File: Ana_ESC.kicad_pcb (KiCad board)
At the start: 4 copper layers, 90 x 90 mm, 105 parts, among them IC3 TCAN330DCNT, J1 BM04B-GHS-TBT_LF__SN__N_, J2 Conn_01x04_Pin, J3 USB_C_Receptacle_USB2.0_16P, J4 BM04B-GHS-TBT_LF__SN__N_, J5 Conn_01x02_Socket, Q10 STL90N6F7, Q11 STL90N6F7, Q12 STL90N6F7, Q7 STL90N6F7, Q8 STL90N6F7, Q9 STL90N6F7, SW1 SW_SPDT, SW2 SW_SPDT, U1 DRV8323RSRGZR, U2 STM32G431CBU6, U3 ME6211C33M5, Y1 ECS-80-20-5PX-TR

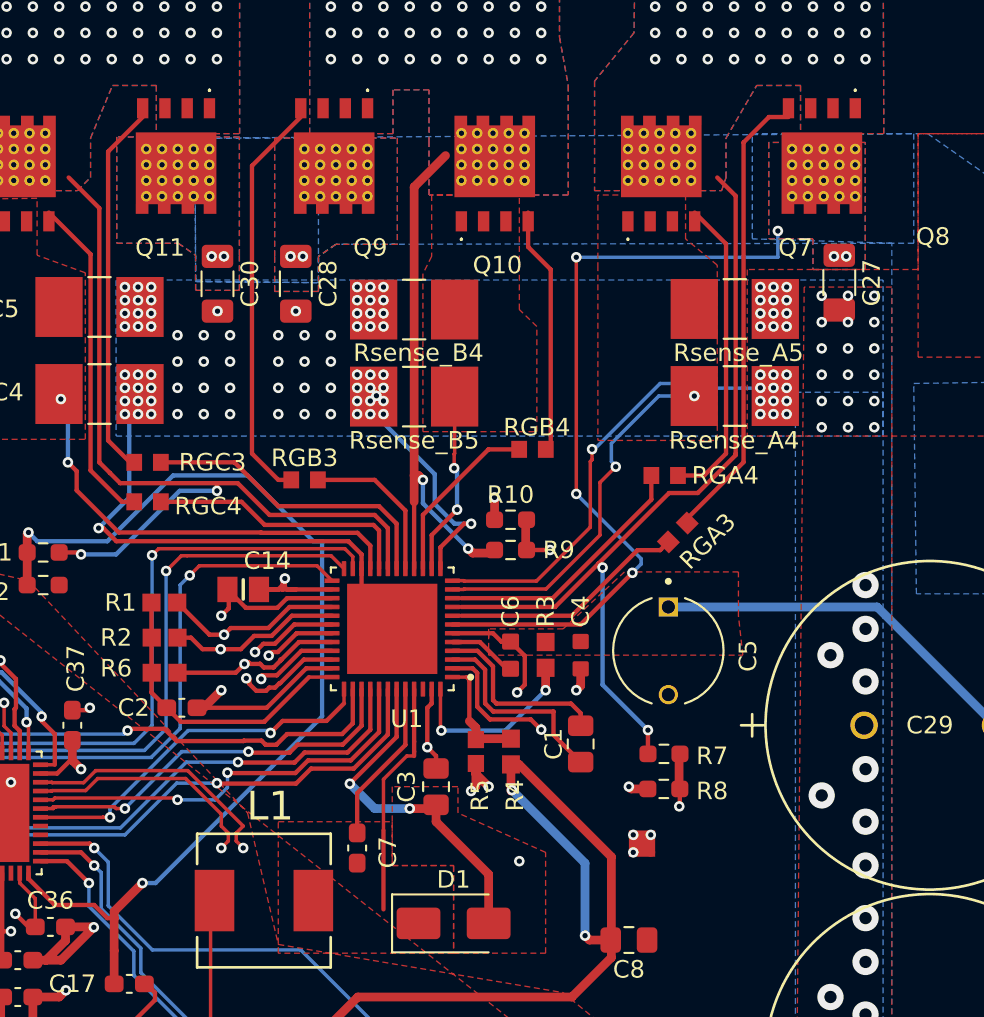
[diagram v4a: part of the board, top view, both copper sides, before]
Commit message: New one_GND_Layer pcb desgin has finished yet. DRC Rule checks needs to be controlling and correcting still.
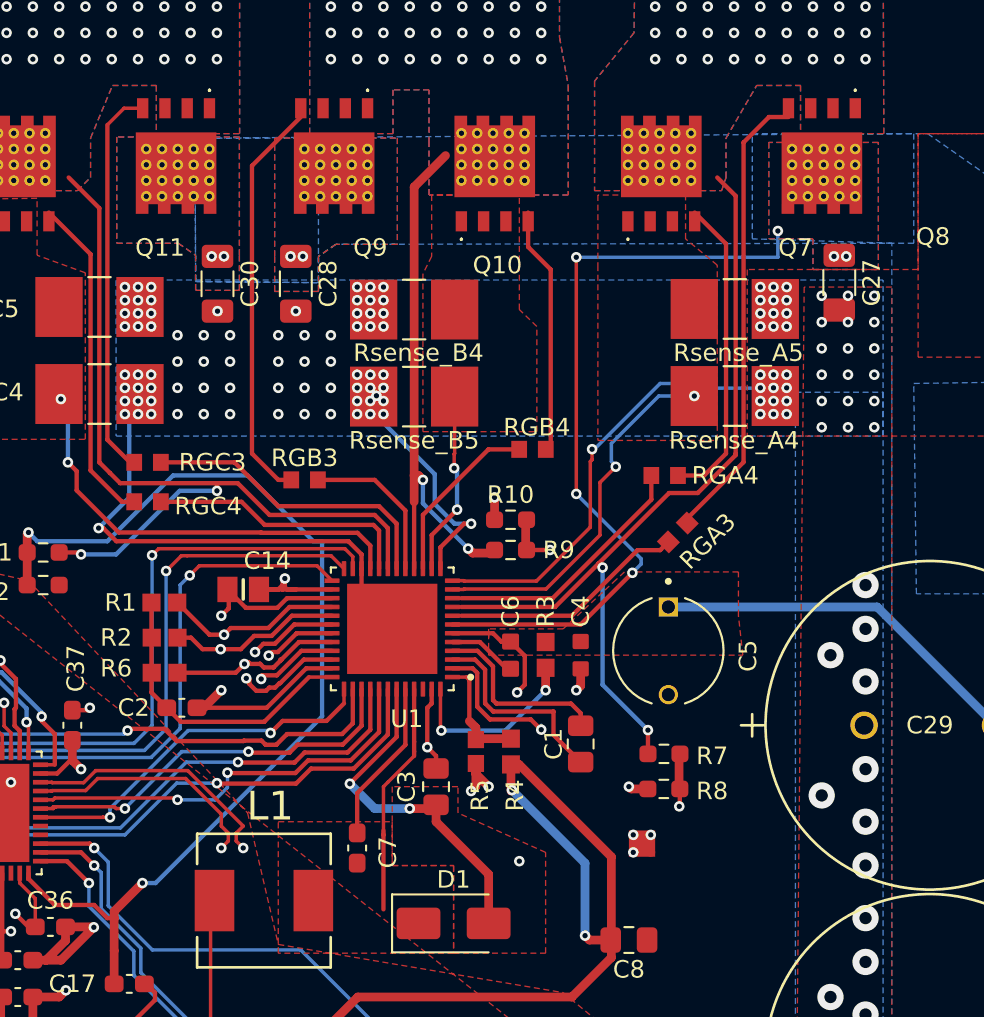
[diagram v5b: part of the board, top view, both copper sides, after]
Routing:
- net Net-(Q11-G): track 21.3 -> 22.5 mm
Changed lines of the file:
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@@
 	)
 	(segment
-		(start 92.25 101.25)
-		(end 91.830761 101.25)
-		(width 0.2)
-		(layer "F.Cu")
-		(net 8)
-	)
-	(segment
 		(start 92.25 100.43905)
 		(end 92.25 101)
@@
 	)
 	(segment
-		(start 90.5 102.580761)
-		(end 90.5 105.5)
+		(start 90.5 105.5)
+		(end 90.5 105.75)
+		(width 0.25)
+		(layer "F.Cu")
+		(net 8)
+	)
+	(segment
+		(start 90.5 103)
+		(end 90.75 102.75)
 		(width 0.2)
 		(layer "F.Cu")
@@
 	)
 	(segment
-		(start 90.5 105.5)
+		(start 90.5 105.75)
 		(end 90.5 110)
 		(width 0.25)
@@
 	)
 	(segment
-		(start 91.830761 101.25)
-		(end 90.5 102.580761)
+		(start 90.5 105.75)
+		(end 90.5 103)
+		(width 0.2)
+		(layer "F.Cu")
+		(net 8)
+	)
+	(segment
+		(start 92.25 101.25)
+		(end 90.75 102.75)
 		(width 0.2)
 		(layer "F.Cu")
@@
 	)
 	(segment
-		(start 74.7918 83.25)
-		(end 74.7918 66.773)
+		(start 76.7148 64.25)
+		(end 76.7648 64.3)
 		(width 0.25)
 		(layer "F.Cu")
@@
 	)
 	(segment
-		(start 74.7918 66.773)
-		(end 76.7648 64.8)
+		(start 76.0418 84.5)
+		(end 74.75 83.2082)
 		(width 0.25)
 		(layer "F.Cu")
@@
 	)
 	(segment
-		(start 76.0418 84.5)
-		(end 74.7918 83.25)
-		(width 0.25)
+		(start 76.7648 64.3)
+		(end 75.7 64.3)
+		(width 0.2)
+		(layer "F.Cu")
+		(net 47)
+	)
+	(segment
+		(start 75.7 64.3)
+		(end 74.75 65.25)
+		(width 0.2)
 		(layer "F.Cu")
 		(net 47)
@@
 	)
 	(segment
+		(start 74.75 83.2082)
+		(end 74.75 65.25)
+		(width 0.25)
+		(layer "F.Cu")
+		(net 47)
+	)
+	(segment
 		(start 83.536085 88.519905)
 		(end 89.019905 88.519905)
@@
 		(layers "F.Cu" "B.Cu" "In1.Cu" "In2.Cu")
 		(hatch edge 0.5)
-		(priority 5)
+		(priority 25)
 		(connect_pads yes
 			(clearance 0.5)
@@
 		(layers "F.Cu" "B.Cu" "In1.Cu" "In2.Cu")
 		(hatch edge 0.5)
-		(priority 5)
+		(priority 25)
 		(connect_pads yes
 			(clearance 0.5)
@@
 		(layers "F.Cu" "B.Cu" "In1.Cu" "In2.Cu")
 		(hatch edge 0.5)
-		(priority 1)
+		(priority 25)
 		(connect_pads yes
 			(clearance 0.5)
@@
 		(polygon
 			(pts
-				(xy 112.4818 66.25) (xy 112.4818 71.75) (xy 115 71.75) (xy 115 73.5) (xy 117.9818 73.5) (xy 117.9818 66.25)
+				(xy 112.4818 66.25) (xy 112.4818 71.75) (xy 115 71.75) (xy 115 73.5) (xy 118.7318 73.5) (xy 118.7318 66.25)
 			)
 		)
@@
 			)
 		)
+	)
+	(zone
+		(net 0)
+		(net_name "")
+		(layer "F.Mask")
+		(hatch edge 0.5)
+		(priority 5)
+		(connect_pads yes
+			(clearance 0.5)
+		)
+		(min_thickness 0.25)
+		(filled_areas_thickness no)
+		(fill yes
+			(thermal_gap 0.5)
+			(thermal_bridge_width 0.5)
+			(smoothing fillet)
+			(radius 0.5)
+			(island_removal_mode 1)
+			(island_area_min 10)
+		)
+		(polygon
+			(pts
+				(xy 100 64.25) (xy 100 68.75) (xy 93.75 68.75) (xy 93.75 64.25)
+			)
+		)
+	)
+	(zone
+		(net 0)
+		(net_name "")
+		(layer "F.Mask")
+		(hatch edge 0.5)
+		(priority 5)
+		(connect_pads yes
+			(clearance 0.5)
+		)
+		(min_thickness 0.25)
+		(filled_areas_thickness no)
+		(fill yes
+			(thermal_gap 0.5)
+			(thermal_bridge_width 0.5)
+			(smoothing fillet)
+			(radius 0.5)
+			(island_removal_mode 1)
+			(island_area_min 10)
+		)
+		(polygon
+			(pts
+				(xy 81.75 66.650284) (xy 81.75 71.150284) (xy 75.5 71.150284) (xy 75.5 66.650284)
+			)
+		)
+	)
+	(zone
+		(net 0)
+		(net_name "")
+		(layer "F.Mask")
+		(hatch edge 0.5)
+		(priority 5)
+		(connect_pads yes
+			(clearance 0.5)
+		)
+		(min_thickness 0.25)
+		(filled_areas_thickness no)
+		(fill yes
+			(thermal_gap 0.5)
+			(thermal_bridge_width 0.5)
+			(smoothing fillet)
+			(radius 0.5)
+			(island_removal_mode 1)
+			(island_area_min 10)
+		)
+		(polygon
+			(pts
+				(xy 72.562969 64.25) (xy 72.562969 68.75) (xy 66.312969 68.75) (xy 66.312969 64.25)
+			)
+		)
+	)
+	(zone
+		(net 0)
+		(net_name "")
+		(layer "F.Mask")
+		(hatch edge 0.5)
+		(priority 5)
+		(connect_pads yes
+			(clearance 0.5)
+		)
+		(min_thickness 0.25)
+		(filled_areas_thickness no)
+		(fill yes
+			(thermal_gap 0.5)
+			(thermal_bridge_width 0.5)
+			(smoothing fillet)
+			(radius 0.5)
+			(island_removal_mode 1)
+			(island_area_min 10)
+		)
+		(polygon
+			(pts
+				(xy 109.5 64.25) (xy 109.5 68.75) (xy 103.25 68.75) (xy 103.25 64.25)
+			)
+		)
+	)
+	(zone
+		(net 0)
+		(net_name "")
+		(layer "F.Mask")
+		(hatch edge 0.5)
+		(priority 5)
+		(connect_pads yes
+			(clearance 0.5)
+		)
+		(min_thickness 0.25)
+		(filled_areas_thickness no)
+		(fill yes
+			(thermal_gap 0.5)
+			(thermal_bridge_width 0.5)
+			(smoothing fillet)
+			(radius 0.5)
+			(island_removal_mode 1)
+			(island_area_min 10)
+		)
+		(polygon
+			(pts
+				(xy 118.75 66.452001) (xy 118.75 70.952001) (xy 112.5 70.952001) (xy 112.5 66.452001)
+			)
+		)
+	)
+	(zone
+		(net 0)
+		(net_name "")
+		(layer "F.Mask")
+		(hatch edge 0.5)
+		(priority 5)
+		(connect_pads yes
+			(clearance 0.5)
+		)
+		(min_thickness 0.25)
+		(filled_areas_thickness no)
+		(fill yes
+			(thermal_gap 0.5)
+			(thermal_bridge_width 0.5)
+			(smoothing fillet)
+			(radius 0.5)
+			(island_removal_mode 1)
+			(island_area_min 10)
+		)
+		(polygon
+			(pts
+				(xy 90.75 66.668644) (xy 90.75 71.168644) (xy 84.5 71.168644) (xy 84.5 66.668644)
+			)
+		)
